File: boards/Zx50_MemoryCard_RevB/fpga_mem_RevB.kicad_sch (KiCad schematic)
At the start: 72 parts, among them J10 DEBUG, J8 JTAG, J9 RJ45_RB1-125B8G1A, U11 LCMXO2-1200HC-4TG144C, U12 CY7C1049DV33, U13 CY7C1049DV33, U14 SST39SF040_TSOP32

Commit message: tweeks before refitting with quartus
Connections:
- net RX_CLK_FLT_N: now also C19.1, R8.2, U11.133 (PT11A); no longer C15.1, R8.1, U11.132 (PT11B)
- net RX_CLK_FLT_P: now also C15.1, R8.1, U11.132 (PT11B); no longer C19.1, R8.2, U11.133 (PT11A)
- net RX_CLK_N: now also C19.2; no longer C15.2
- net RX_CLK_P: now also C15.2; no longer C19.2
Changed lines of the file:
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@@
 	)
 	(label "RX_CLK_FLT_N"
-		(at 128.27 210.82 0)
+		(at 128.27 208.28 0)
 		(effects
 			(font
@@
 	)
 	(label "RX_CLK_FLT_P"
-		(at 128.27 208.28 0)
+		(at 128.27 210.82 0)
 		(effects
 			(font
@@
 	)
 	(label "RX_CLK_P"
-		(at 153.67 208.28 0)
+		(at 153.67 210.82 0)
 		(effects
 			(font
@@
 	)
 	(label "RX_CLK_N"
-		(at 153.67 210.82 0)
-		(effects
-			(font
+		(at 153.67 208.28 0)
+		(effects
+			(font

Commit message: more work on revb memory card, plus a diag program for rev a1.
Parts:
- R12, R14, R15, R17: footprint Resistor_SMD:R_0805_2012Metric -> Resistor_SMD:R_0402_1005Metric; LCSC C17414 -> C25744; MFG_PN 0805W8F1002T5E -> 0402W8F1002T5E
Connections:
- net RX_DAT_FLT_N: now also C20.1, R9.2, U11.122 (PT15A); no longer C16.1, R9.1, U11.121 (PT15B)
- net RX_DAT_FLT_P: now also C16.1, R9.1, U11.121 (PT15B); no longer C20.1, R9.2, U11.122 (PT15A)
- net RX_DAT_N: now also C20.2; no longer C16.2
- net RX_DAT_P: now also C16.2; no longer C20.2
- net TX_CLK_FLT_N: now also C18.1, U11.111 (PT17B); no longer C17.1, U11.115 (PT16B)
- net TX_CLK_FLT_P: now also C22.1, U11.112 (PT17A); no longer C21.1, U11.117 (PT16A)
- net TX_CLK_N: now also C18.2; no longer C17.2
- net TX_CLK_P: now also C22.2; no longer C21.2
- net TX_DAT_FLT_N: now also C21.1, U11.117 (PT16A); no longer C18.1, U11.111 (PT17B)
- net TX_DAT_FLT_P: now also C17.1, U11.115 (PT16B); no longer C22.1, U11.112 (PT17A)
- net TX_DAT_N: now also C21.2; no longer C18.2
- net TX_DAT_P: now also C17.2; no longer C22.2

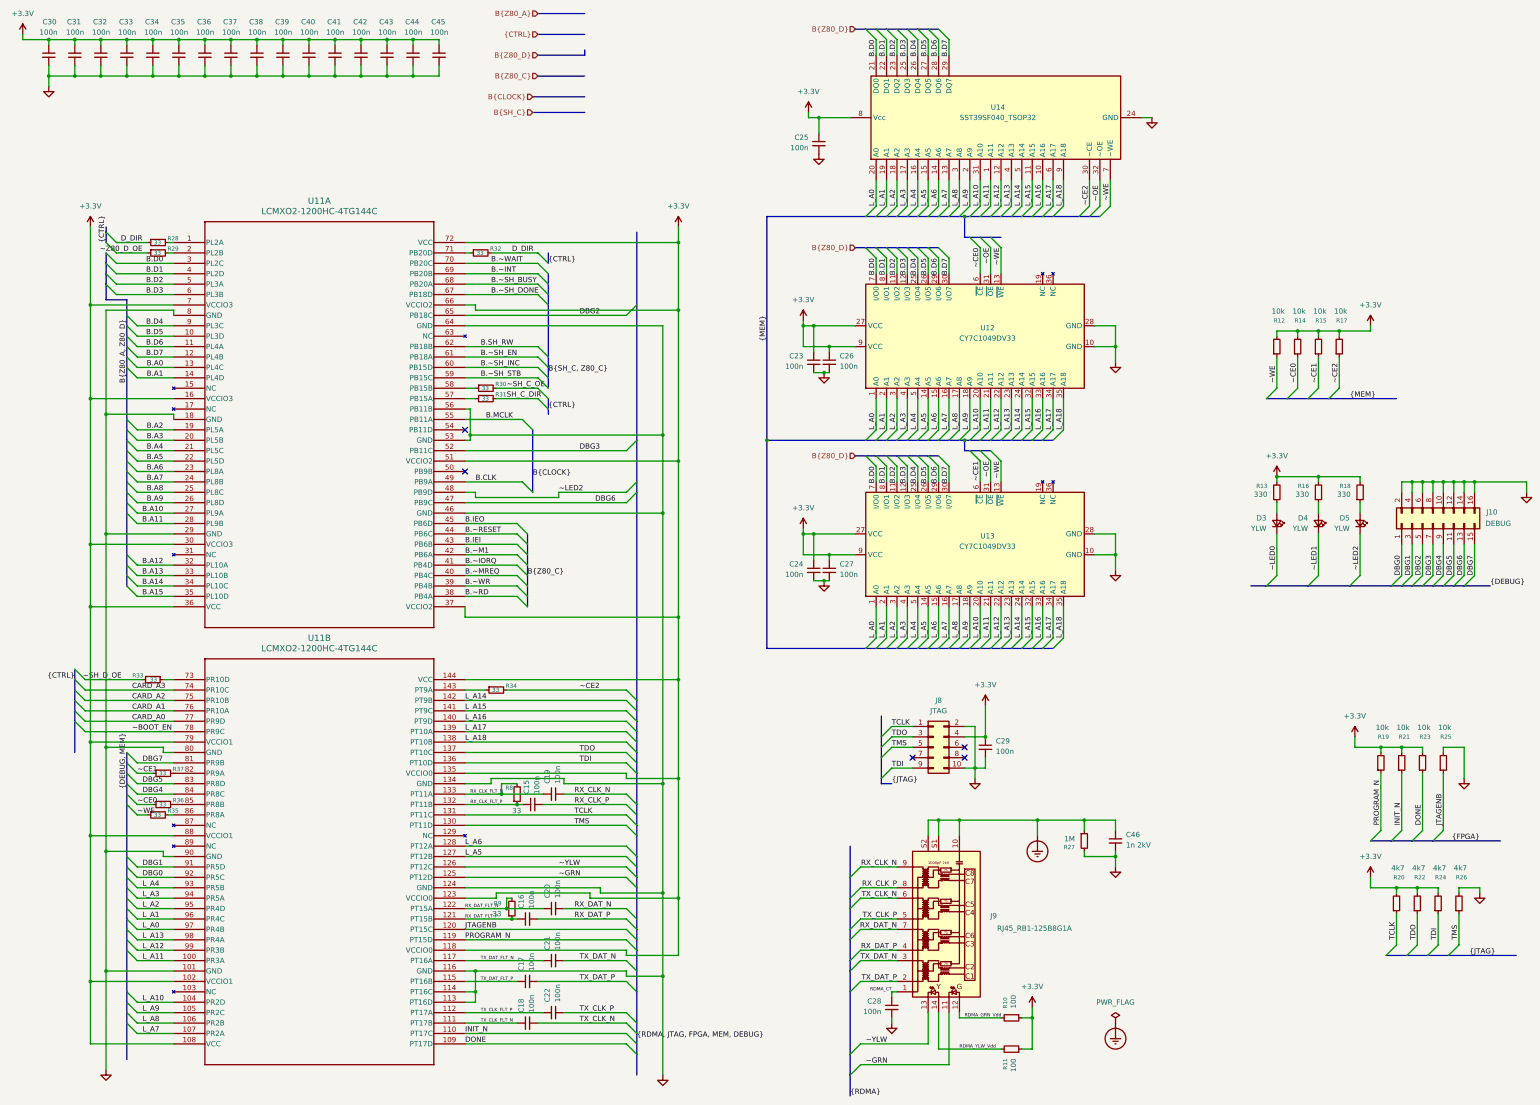
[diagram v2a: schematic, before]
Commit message: fixup pic z80 timing.  add memory test script to pico
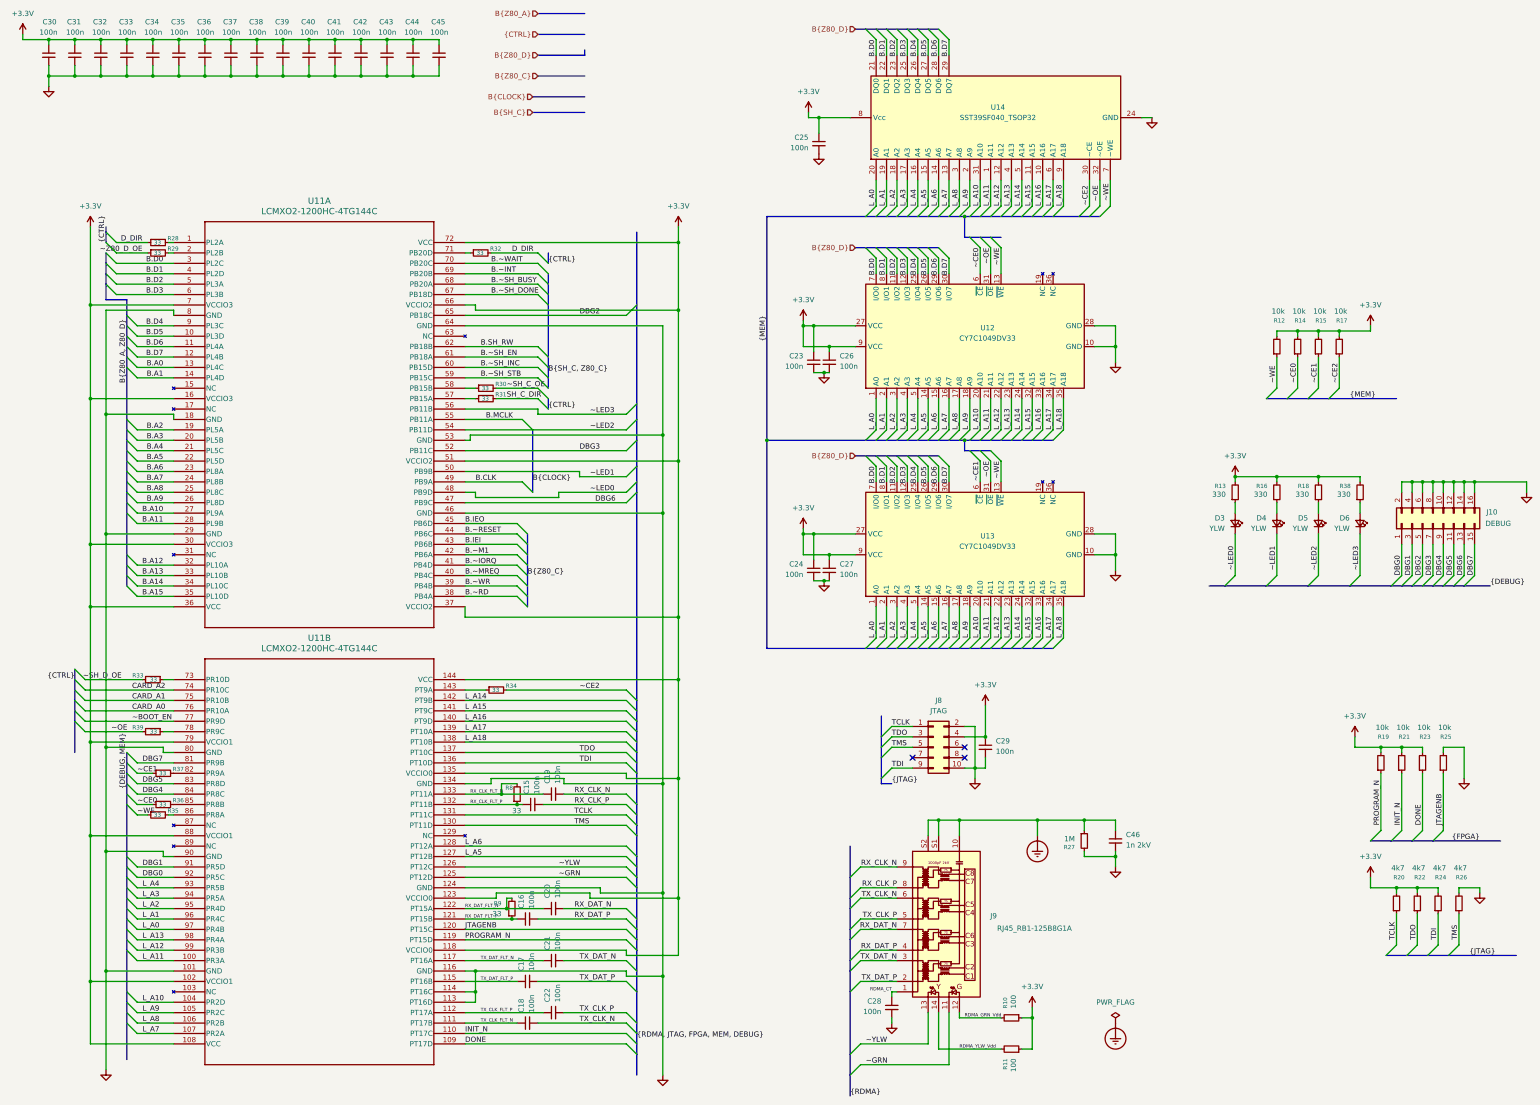
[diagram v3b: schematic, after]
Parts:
- added D6: YLW, LED_SMD:LED_0805_2012Metric, symbol Device:LED_Small
- added R38: 330, Resistor_SMD:R_0805_2012Metric, symbol Device:R_Small
- added R39: 33, Resistor_SMD:R_0402_1005Metric, symbol Device:R_Small
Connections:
- net CARD_A3 is gone; now on net CARD_A2: U11.74 (PR10C)
- net +3.3V: now also R38.2
- net CARD_A0: now also U11.76 (PR10A); no longer U11.77 (PR9D)
- net CARD_A1: now also U11.75 (PR10B); no longer U11.76 (PR10A)
- net CARD_A2: no longer U11.75 (PR10B)
- net GND: no longer U11.56 (PB11B)
- net ~BOOT_EN: now also U11.77 (PR9D); no longer U11.78 (PR9C)
- net ~LED0: now also U11.48 (PB9D)
- net ~LED1: now also U11.50 (PB9B)
- net ~LED2: now also U11.54 (PB11D); no longer U11.48 (PB9D)
- net ~OE: now also R39.2
- new net: D6.2 (A), R38.1
- new net: R39.1, U11.78 (PR9C)
- new net ~LED3: D6.1 (K), U11.56 (PB11B)
- no-connect marks 5 -> 3
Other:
- moved on the sheet: D3, D4, D5, R13, R16, R18
